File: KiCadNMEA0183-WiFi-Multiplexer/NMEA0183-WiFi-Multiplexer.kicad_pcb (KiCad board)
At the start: 2 copper layers, 40 x 55.2 mm, 8 parts, among them J1 NMEA In, J2 NMEA In, U1 WeMos_D1_mini, U2 MAX232

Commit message: Add files via upload
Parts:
- added J3: Power, TerminalBlock:TerminalBlock_bornier-2_P5.08mm, F.Cu at (71.1, 66.0)
- added U3: R-78E50-10_TO220, Package_TO_SOT_THT:TO-220-3_Vertical, F.Cu at (84.5, 63.5)
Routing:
- net +5V: track 39.0 -> 84.7 mm
- net GND: track 116.1 -> 137.4 mm
- net Net-(J3-Pad2): track 0.00 -> 14.4 mm
- net (no net): track 0.00 -> 0.64 mm
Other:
- board size 40 x 55.2 mm -> 40 x 67.3 mm
- board text added: "+"
- board text added: "-"
- board text added: "In 1"
- board text added: "In 2"

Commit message: Add files via upload
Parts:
- moved U3 2.29 mm to (86.4, 64.8)
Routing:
- net Net-(J3-Pad2): track 14.4 -> 16.8 mm
- net GND: track 137.4 -> 135.1 mm
- net +5V: track 84.7 -> 82.6 mm
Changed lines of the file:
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@@
     (thickness 1.6)
     (drawings 16)
-    (tracks 86)
+    (tracks 87)
     (zones 0)
     (modules 10)
@@
   )
   (module Package_TO_SOT_THT:TO-220-3_Vertical (layer F.Cu)
-    (at 84.455 63.5)
+    (at 86.36 64.77)
     (descr "TO-220-3, Vertical, RM 2.54mm, see https://www.vishay.com/docs/66542/to-220-1.pdf")
     (tags "TO-220-3 Vertical RM 2.54mm")
@@
     (descr "CP, Radial series, Radial, pin pitch=2.50mm, , diameter=6.3mm, Electrolytic Capacitor")
     (tags "CP Radial series Radial pin pitch 2.50mm  diameter 6.3mm Electrolytic Capacitor")
-    (fp_text reference C4 (at 1.25 -4.4 90) (layer F.SilkS)
+    (fp_text reference C4 (at -3.175 0 180) (layer F.SilkS)
       (effects (font (size 1 1) (thickness 0.15)))
     )
@@
       (effects (font (size 1 1) (thickness 0.15)))
     )
-    (fp_text user %R (at -3.175 -0.635 180) (layer F.Fab)
+    (fp_text user %R (at 2.54 1.905 180) (layer F.Fab)
       (effects (font (size 1 1) (thickness 0.15)))
     )
@@
   (segment (start 75.565 66.04) (end 71.12 66.04) (width 0.25) (layer F.Cu) (net 1))
   (segment (start 79.375 69.85) (end 75.565 66.04) (width 0.25) (layer F.Cu) (net 1))
-  (segment (start 86.995 63.5) (end 86.995 71.755) (width 0.25) (layer F.Cu) (net 1))
   (segment (start 87.63 71.755) (end 86.995 71.755) (width 0.25) (layer F.Cu) (net 1))
   (segment (start 86.995 71.755) (end 80.645 71.755) (width 0.25) (layer F.Cu) (net 1))
+  (segment (start 88.9 64.77) (end 88.9 67.945) (width 0.25) (layer F.Cu) (net 1))
+  (segment (start 88.9 67.945) (end 90.805 69.85) (width 0.25) (layer F.Cu) (net 1))
   (segment (start 79.375 78.105) (end 79.375 75.565) (width 0.25) (layer B.Cu) (net 2))
   (segment (start 93.98 79.375) (end 80.645 79.375) (width 0.25) (layer B.Cu) (net 2))
@@
   (segment (start 91.394998 99.105002) (end 91.44 99.105002) (width 0.25) (layer F.Cu) (net 16))
   (segment (start 91.44 93.345) (end 92.075 92.71) (width 0.25) (layer F.Cu) (net 16))
-  (segment (start 100.33 90.17) (end 97.79 90.17) (width 0.25) (layer B.Cu) (net 16))
-  (segment (start 105.41 85.09) (end 100.33 90.17) (width 0.25) (layer B.Cu) (net 16))
-  (segment (start 105.41 66.04) (end 105.41 85.09) (width 0.25) (layer B.Cu) (net 16))
-  (segment (start 89.535 63.5) (end 102.87 63.5) (width 0.25) (layer B.Cu) (net 16))
-  (segment (start 102.87 63.5) (end 105.41 66.04) (width 0.25) (layer B.Cu) (net 16))
+  (segment (start 105.41 65.405) (end 104.775 64.77) (width 0.25) (layer B.Cu) (net 16))
+  (segment (start 105.41 85.09) (end 105.41 65.405) (width 0.25) (layer B.Cu) (net 16))
+  (segment (start 104.775 64.77) (end 91.44 64.77) (width 0.25) (layer B.Cu) (net 16))
+  (segment (start 97.79 90.17) (end 100.33 90.17) (width 0.25) (layer B.Cu) (net 16))
+  (segment (start 100.33 90.17) (end 105.41 85.09) (width 0.25) (layer B.Cu) (net 16))
   (segment (start 80.01 91.30137) (end 80.01 95.25) (width 0.25) (layer B.Cu) (net 18))
   (segment (start 80.01 90.17) (end 80.01 91.30137) (width 0.25) (layer B.Cu) (net 18))
@@
   (segment (start 83.84 92.71) (end 82.55 94) (width 0.25) (layer B.Cu) (net 19))
   (segment (start 86.22137 92.71) (end 83.84 92.71) (width 0.25) (layer B.Cu) (net 19))
+  (segment (start 81.915 64.77) (end 86.36 64.77) (width 0.25) (layer F.Cu) (net 29))
   (segment (start 71.12 60.96) (end 78.105 60.96) (width 0.25) (layer F.Cu) (net 29))
-  (segment (start 80.645 63.5) (end 84.455 63.5) (width 0.25) (layer F.Cu) (net 29))
-  (segment (start 78.105 60.96) (end 80.645 63.5) (width 0.25) (layer F.Cu) (net 29))
+  (segment (start 78.105 60.96) (end 81.915 64.77) (width 0.25) (layer F.Cu) (net 29))
 )

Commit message: Add files via upload
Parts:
- moved J3 0.63 mm to (71.1, 66.7)
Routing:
- net GND: track 135.1 -> 131.9 mm
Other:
- board text added: "S1"
- board text added: "S2"
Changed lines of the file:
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@@
   (general
     (thickness 1.6)
-    (drawings 16)
+    (drawings 20)
     (tracks 87)
     (zones 0)
@@
   )
   (module TerminalBlock:TerminalBlock_bornier-2_P5.08mm (layer F.Cu)
-    (at 71.12 66.04 90)
+    (at 71.12 66.675 90)
     (descr "simple 2-pin terminal block, pitch 5.08mm, revamped version of bornier2")
     (tags "terminal block bornier2")
-    (fp_text reference J3 (at -1.27 -2.54 90) (layer F.SilkS)
+    (fp_text reference J3 (at -1.27 -2.54 -90) (layer F.SilkS)
       (effects (font (size 1 1) (thickness 0.15)))
     )
@@
     (descr "simple 2-pin terminal block, pitch 5.08mm, revamped version of bornier2")
     (tags "terminal block bornier2")
-    (fp_text reference J2 (at -1.27 -2.54 90) (layer F.SilkS)
+    (fp_text reference J2 (at -1.27 -2.54 -90) (layer F.SilkS)
       (effects (font (size 1 1) (thickness 0.15)))
     )
@@
     (descr "simple 2-pin terminal block, pitch 5.08mm, revamped version of bornier2")
     (tags "terminal block bornier2")
-    (fp_text reference J1 (at -1.27 -2.54 90) (layer F.SilkS)
+    (fp_text reference J1 (at -1.27 -2.54 -90) (layer F.SilkS)
       (effects (font (size 1 1) (thickness 0.15)))
     )
@@
     )
   )
+  (gr_text S2 (at 76.2 71.12 270) (layer F.SilkS)
+    (effects (font (size 1 1) (thickness 0.15)))
+  )
+  (gr_text S1 (at 76.2 82.55 270) (layer F.SilkS)
+    (effects (font (size 1 1) (thickness 0.15)))
+  )
+  (gr_text - (at 76.2 91.44 90) (layer F.SilkS)
+    (effects (font (size 1 1) (thickness 0.15)))
+  )
+  (gr_text - (at 76.2 80.01 90) (layer F.SilkS)
+    (effects (font (size 1 1) (thickness 0.15)))
+  )
   (gr_text "In 1" (at 68.58 86.36 270) (layer F.SilkS)
     (effects (font (size 1 1) (thickness 0.15)))
@@
     (effects (font (size 1 1) (thickness 0.15)))
   )
-  (gr_text - (at 76.835 66.04 90) (layer F.SilkS)
+  (gr_text - (at 76.2 67.31 90) (layer F.SilkS)
     (effects (font (size 1 1) (thickness 0.15)))
   )
-  (gr_text + (at 76.835 60.96) (layer F.SilkS)
+  (gr_text + (at 76.2 60.96) (layer F.SilkS)
     (effects (font (size 1 1) (thickness 0.15)))
   )
@@
   (segment (start 68.58 88.745) (end 69.37 89.535) (width 0.25) (layer B.Cu) (net 1))
   (segment (start 68.58 78.895) (end 68.58 88.745) (width 0.25) (layer B.Cu) (net 1))
-  (segment (start 79.375 73.065) (end 79.375 69.85) (width 0.25) (layer F.Cu) (net 1))
-  (segment (start 75.565 66.04) (end 71.12 66.04) (width 0.25) (layer F.Cu) (net 1))
-  (segment (start 79.375 69.85) (end 75.565 66.04) (width 0.25) (layer F.Cu) (net 1))
   (segment (start 87.63 71.755) (end 86.995 71.755) (width 0.25) (layer F.Cu) (net 1))
   (segment (start 86.995 71.755) (end 80.645 71.755) (width 0.25) (layer F.Cu) (net 1))
   (segment (start 88.9 64.77) (end 88.9 67.945) (width 0.25) (layer F.Cu) (net 1))
   (segment (start 88.9 67.945) (end 90.805 69.85) (width 0.25) (layer F.Cu) (net 1))
+  (segment (start 76.795 73.065) (end 76.795 70.445) (width 0.25) (layer F.Cu) (net 1))
+  (segment (start 73.025 66.675) (end 71.12 66.675) (width 0.25) (layer F.Cu) (net 1))
+  (segment (start 76.795 70.445) (end 73.025 66.675) (width 0.25) (layer F.Cu) (net 1))
   (segment (start 79.375 78.105) (end 79.375 75.565) (width 0.25) (layer B.Cu) (net 2))
   (segment (start 93.98 79.375) (end 80.645 79.375) (width 0.25) (layer B.Cu) (net 2))
@@
   (segment (start 86.22137 92.71) (end 83.84 92.71) (width 0.25) (layer B.Cu) (net 19))
   (segment (start 81.915 64.77) (end 86.36 64.77) (width 0.25) (layer F.Cu) (net 29))
-  (segment (start 71.12 60.96) (end 78.105 60.96) (width 0.25) (layer F.Cu) (net 29))
-  (segment (start 78.105 60.96) (end 81.915 64.77) (width 0.25) (layer F.Cu) (net 29))
+  (segment (start 81.915 64.77) (end 78.74 61.595) (width 0.25) (layer F.Cu) (net 29))
+  (segment (start 78.74 61.595) (end 71.12 61.595) (width 0.25) (layer F.Cu) (net 29))
 )

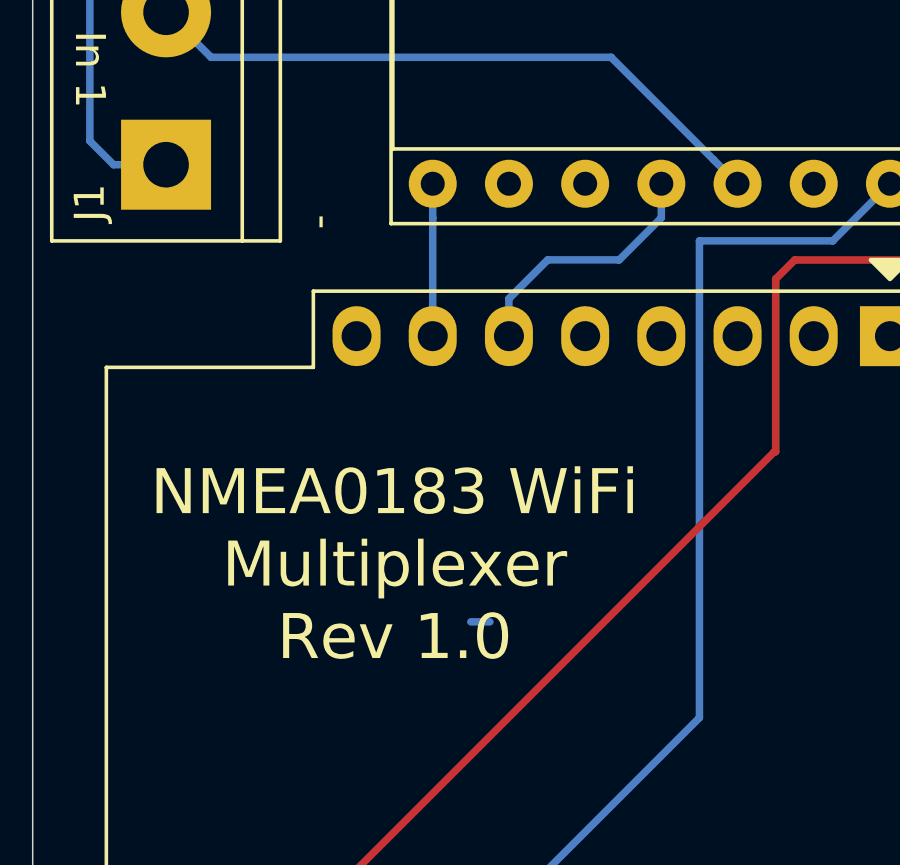
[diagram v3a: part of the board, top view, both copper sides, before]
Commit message: Version 1.1 (Changed to D7/D2 pins to avoid boot problems).
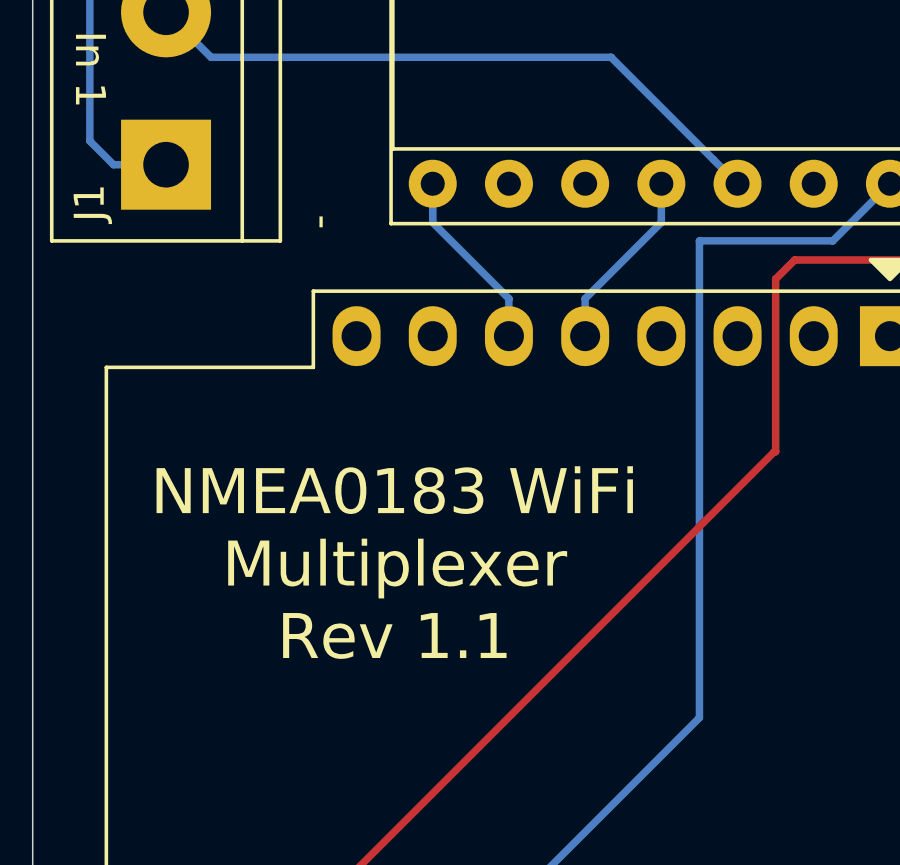
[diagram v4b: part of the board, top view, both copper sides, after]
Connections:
- U2 pad 12: Net-(U1-Pad6) -> Net-(U1-Pad5)
- U2 pad 9: Net-(U1-Pad7) -> Net-(U1-Pad6)
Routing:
- net Net-(U1-Pad5): track 0.00 -> 6.13 mm
- net Net-(U1-Pad7): track 5.08 -> 0.00 mm
- net Net-(U1-Pad6): track 8.58 -> 6.13 mm
- net (no net): track 0.64 -> 0.00 mm
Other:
- board text added: "NMEA0183 WiFi Multiplexer Rev 1.1"
- board text removed: "NMEA0183 WiFi Multiplexer Rev 1.0"
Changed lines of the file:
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@@
     (thickness 1.6)
     (drawings 20)
-    (tracks 87)
+    (tracks 85)
     (zones 0)
     (modules 10)
@@
       (net 3 "Net-(C2-Pad2)"))
     (pad 12 thru_hole oval (at 7.62 10.16 270) (size 1.6 1.6) (drill 0.8) (layers *.Cu *.Mask)
-      (net 19 "Net-(U1-Pad6)"))
+      (net 20 "Net-(U1-Pad5)"))
     (pad 4 thru_hole oval (at 0 7.62 270) (size 1.6 1.6) (drill 0.8) (layers *.Cu *.Mask)
       (net 4 "Net-(C2-Pad1)"))
@@
       (net 2 "Net-(C1-Pad1)"))
     (pad 9 thru_hole oval (at 7.62 17.78 270) (size 1.6 1.6) (drill 0.8) (layers *.Cu *.Mask)
-      (net 18 "Net-(U1-Pad7)"))
+      (net 19 "Net-(U1-Pad6)"))
     (pad 1 thru_hole rect (at 0 0 270) (size 1.6 1.6) (drill 0.8) (layers *.Cu *.Mask)
       (net 7 "Net-(C4-Pad1)"))
@@
   (gr_line (start 66.675 55.88) (end 106.68 55.88) (layer Edge.Cuts) (width 0.05))
   (gr_line (start 66.675 67.945) (end 66.675 55.88) (layer Edge.Cuts) (width 0.05))
-  (gr_text "NMEA0183 WiFi\nMultiplexer\nRev 1.0" (at 78.74 102.87) (layer F.SilkS)
+  (gr_text "NMEA0183 WiFi\nMultiplexer\nRev 1.1" (at 78.74 102.87) (layer F.SilkS)
     (effects (font (size 1.5 1.5) (thickness 0.3)))
   )
@@
   (gr_line (start 66.675 67.945) (end 66.675 123.19) (layer Edge.Cuts) (width 0.05))
   (gr_line (start 106.68 122.555) (end 106.68 67.945) (layer Edge.Cuts) (width 0.05))
-  (segment (start 81.28 104.775) (end 81.915 104.775) (width 0.25) (layer B.Cu) (net 0))
   (segment (start 88.9 107.97) (end 88.9 92.075) (width 0.25) (layer B.Cu) (net 1))
   (segment (start 88.9 92.075) (end 93.345 92.075) (width 0.25) (layer B.Cu) (net 1))
@@
   (segment (start 97.79 90.17) (end 100.33 90.17) (width 0.25) (layer B.Cu) (net 16))
   (segment (start 100.33 90.17) (end 105.41 85.09) (width 0.25) (layer B.Cu) (net 16))
-  (segment (start 80.01 91.30137) (end 80.01 95.25) (width 0.25) (layer B.Cu) (net 18))
-  (segment (start 80.01 90.17) (end 80.01 91.30137) (width 0.25) (layer B.Cu) (net 18))
-  (segment (start 87.63 91.30137) (end 86.22137 92.71) (width 0.25) (layer B.Cu) (net 19))
-  (segment (start 87.63 90.17) (end 87.63 91.30137) (width 0.25) (layer B.Cu) (net 19))
-  (segment (start 82.55 94) (end 82.55 95.25) (width 0.25) (layer B.Cu) (net 19))
-  (segment (start 83.84 92.71) (end 82.55 94) (width 0.25) (layer B.Cu) (net 19))
-  (segment (start 86.22137 92.71) (end 83.84 92.71) (width 0.25) (layer B.Cu) (net 19))
+  (segment (start 80.01 91.46) (end 80.01 90.17) (width 0.25) (layer B.Cu) (net 19))
+  (segment (start 82.55 95.25) (end 82.55 94) (width 0.25) (layer B.Cu) (net 19))
+  (segment (start 82.55 94) (end 80.01 91.46) (width 0.25) (layer B.Cu) (net 19))
+  (segment (start 87.63 91.46) (end 87.63 90.17) (width 0.25) (layer B.Cu) (net 20))
+  (segment (start 85.09 95.25) (end 85.09 94) (width 0.25) (layer B.Cu) (net 20))
+  (segment (start 85.09 94) (end 87.63 91.46) (width 0.25) (layer B.Cu) (net 20))
   (segment (start 81.915 64.77) (end 86.36 64.77) (width 0.25) (layer F.Cu) (net 29))
   (segment (start 81.915 64.77) (end 78.74 61.595) (width 0.25) (layer F.Cu) (net 29))
